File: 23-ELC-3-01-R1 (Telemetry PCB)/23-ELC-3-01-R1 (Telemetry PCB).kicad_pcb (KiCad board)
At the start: 2 copper layers, 56.5 x 65 mm, 117 parts, among them J1 Conn_01x01, J11 LHRE_Component_Library_Raspbe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, J2 Conn_01x02, J3 Conn_01x08, J4 Conn_01x02, J5 Conn_01x02, J6 Conn_01x08, J7 Conn_01x02, J8 Conn_02x11_Top_Bottom, J9 Conn_01x06, SW1 SW_DPDT_x2, U1 LHRE_Component_Library_Adafru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, U10 MCP2515-xSO, U11 SN65HVD230, U2 DS3231M, U3 LMR51420, U4 MCP2515-xSO, U5 SN65HVD230, U6 MCP2515-xSO, U7 SN65HVD230, U8 MCP2515-xSO, U9 SN65HVD230, Y1 16 MHz, Y2 16 MHz, Y3 16 MHz, Y4 16 MHz

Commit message: First draft of layout
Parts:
- removed J2, J4, J5, J7: Conn_01x02, Connector_PinHeader_2.54mm:PinHeader_1x02_P2.54mm_Vertical
- added C29: 1uF, Capacitor_SMD:C_0805_2012Metric_Pad1.18x1.45mm_HandSolder, B.Cu at (131.2, 82.2)
- added C30: 1uF, Capacitor_SMD:C_0805_2012Metric_Pad1.18x1.45mm_HandSolder, B.Cu at (116.7, 82.8)
- C3, C4, C5, C6, C7, C8, F1, L1, R4, R5, R7, R8, R9, U2, U3: moved to B.Cu
- moved C21 253.0 mm to (116.0, 127.4), turned to -90 degrees
- moved TP22 248.7 mm to (133.7, 128.4)
- moved C23 244.4 mm to (146.0, 125.0)
- moved R20 244.2 mm to (116.0, 122.3), turned to -90 degrees
- moved Y3 242.3 mm to (135.1, 120.8), turned to -135 degrees
- moved C5 240.6 mm to (144.4, 81.2)
- moved C8 238.9 mm to (138.8, 77.4)
- moved C19 237.8 mm to (132.1, 122.9), turned to -45 degrees
- moved JP11 237.1 mm to (142.7, 122.3), turned to 90 degrees
- moved JP9 235.3 mm to (130.7, 125.5)
- moved C3 234.7 mm to (144.4, 79.7)
- moved JP10 232.9 mm to (130.7, 128.0), turned to 180 degrees
- moved R7 232.2 mm to (144.4, 88.2)
- moved C22 231.9 mm to (135.6, 126.8), turned to -90 degrees
- moved C4 229.0 mm to (144.4, 78.2)
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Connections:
- J9 pad 4: /TSAL_G -> GND
- J9 pad 5: /TSAL_R -> /TSAL_G
- J9 pad 6: unconnected-(J9-Pad6) -> /TSAL_R
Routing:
- net +3V3: track 0.00 -> 230.6 mm, vias 0 -> 10
- net +5V: track 0.00 -> 162.3 mm, vias 0 -> 4
- net GND: track 0.00 -> 145.8 mm, vias 0 -> 39
- net /GPS_RX: track 0.00 -> 79.6 mm
- net +BATT: track 0.00 -> 70.4 mm
- net /GPS_TX: track 0.00 -> 69.9 mm
- net /CAN_CS_2: track 0.00 -> 66.7 mm, vias 0 -> 3
- net /CAN_MISO_01: track 0.00 -> 56.7 mm, vias 0 -> 4
- net /CAN_CS_3: track 0.00 -> 48.9 mm
- net /TSAL_R: track 0.00 -> 48.4 mm, vias 0 -> 1
- net /CAN_L_1_A: track 0.00 -> 46.5 mm, vias 0 -> 2
- net /CAN_SCK_01: track 0.00 -> 45.8 mm, vias 0 -> 3
- net /CAN_CS_0: track 0.00 -> 44.1 mm, vias 0 -> 3
- net /CAN_MISO_23: track 0.00 -> 43.3 mm, vias 0 -> 3
- net /CAN_H_1: track 0.00 -> 41.6 mm, vias 0 -> 2
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- added copper zone on B.Cu, net GND

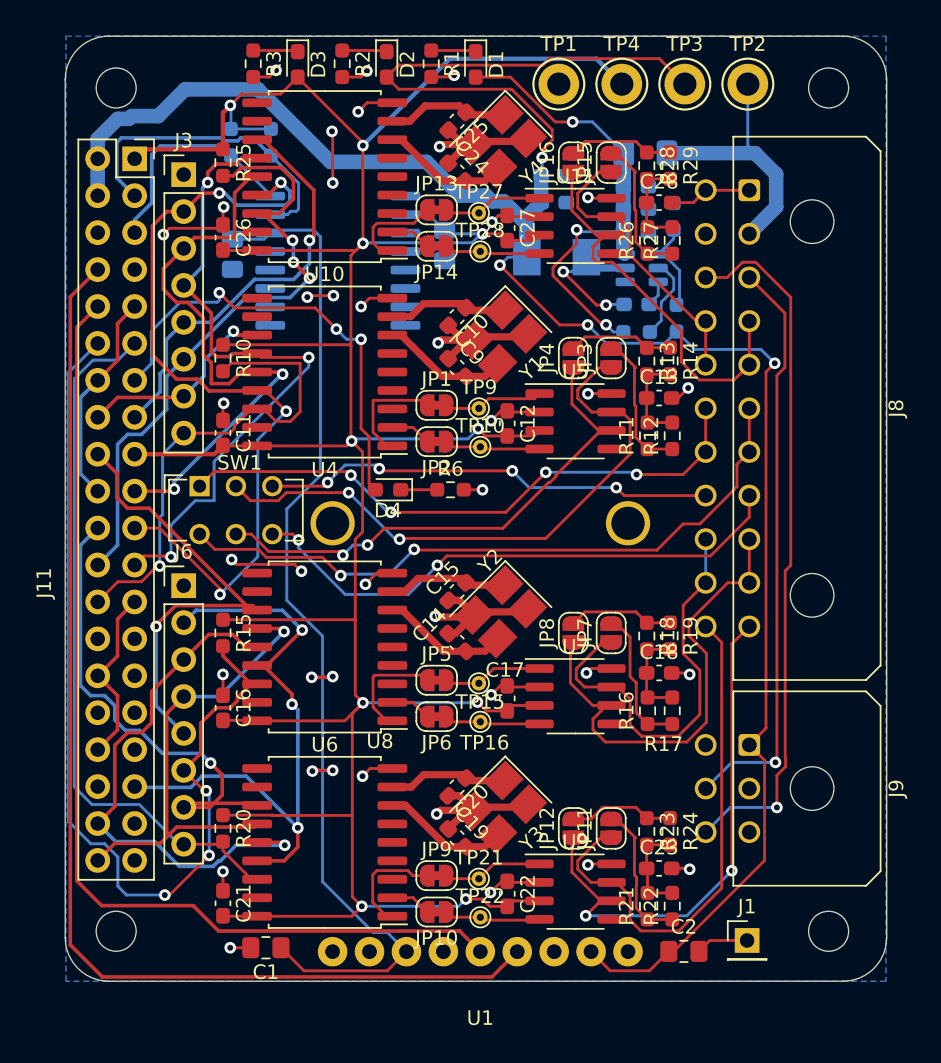
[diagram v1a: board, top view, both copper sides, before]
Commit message: Fixed review notes and made 4 layer
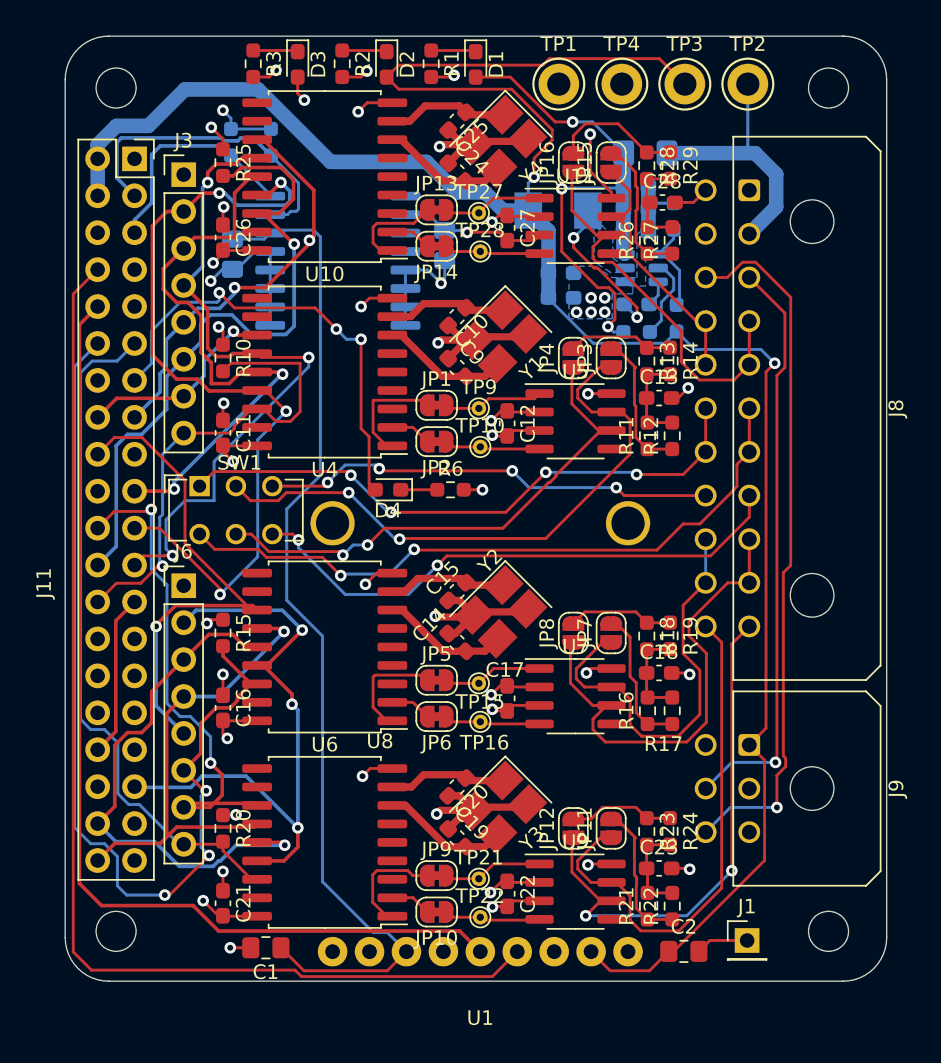
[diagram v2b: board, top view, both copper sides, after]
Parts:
- moved C8 6.72 mm to (139.2, 84.1)
- moved C7 6.57 mm to (139.2, 85.8)
- moved L1 3.20 mm to (139.1, 79.8)
- moved C28 0.23 mm to (146.2, 79.2)
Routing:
- net +3V3: track 230.6 -> 47.0 mm, vias 10 -> 14
- net GND: track 145.8 -> 135.6 mm, vias 39 -> 35
- net +5V: track 162.3 -> 154.7 mm, vias 4 -> 2
- net /Buck 24 to 5/V_in: track 32.9 -> 36.5 mm
- net /CAN_INT_2: track 32.3 -> 34.8 mm
- net /Buck 24 to 5/SW: track 10.1 -> 12.6 mm
- net /CAN_CS_0: track 44.1 -> 46.3 mm, vias 3 -> 1
- net /CAN_H_0: track 19.9 -> 18.0 mm
- net Net-(JP16-Pad2): track 7.30 -> 9.01 mm
- net /CAN_CS_3: track 48.9 -> 47.7 mm
- net /CAN_SCK_01: track 45.8 -> 46.6 mm
- net /CAN_INT_3: track 33.8 -> 34.5 mm, vias 1 -> 2
- net /CAN_INT_0: track 28.8 -> 28.2 mm, vias 1 -> 2
- added copper zone on In2.Cu, net +3V3
- added copper zone on B.Cu, net /Buck 24 to 5/SW
- added copper zone on In1.Cu, net GND
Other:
- copper layers 2 -> 4

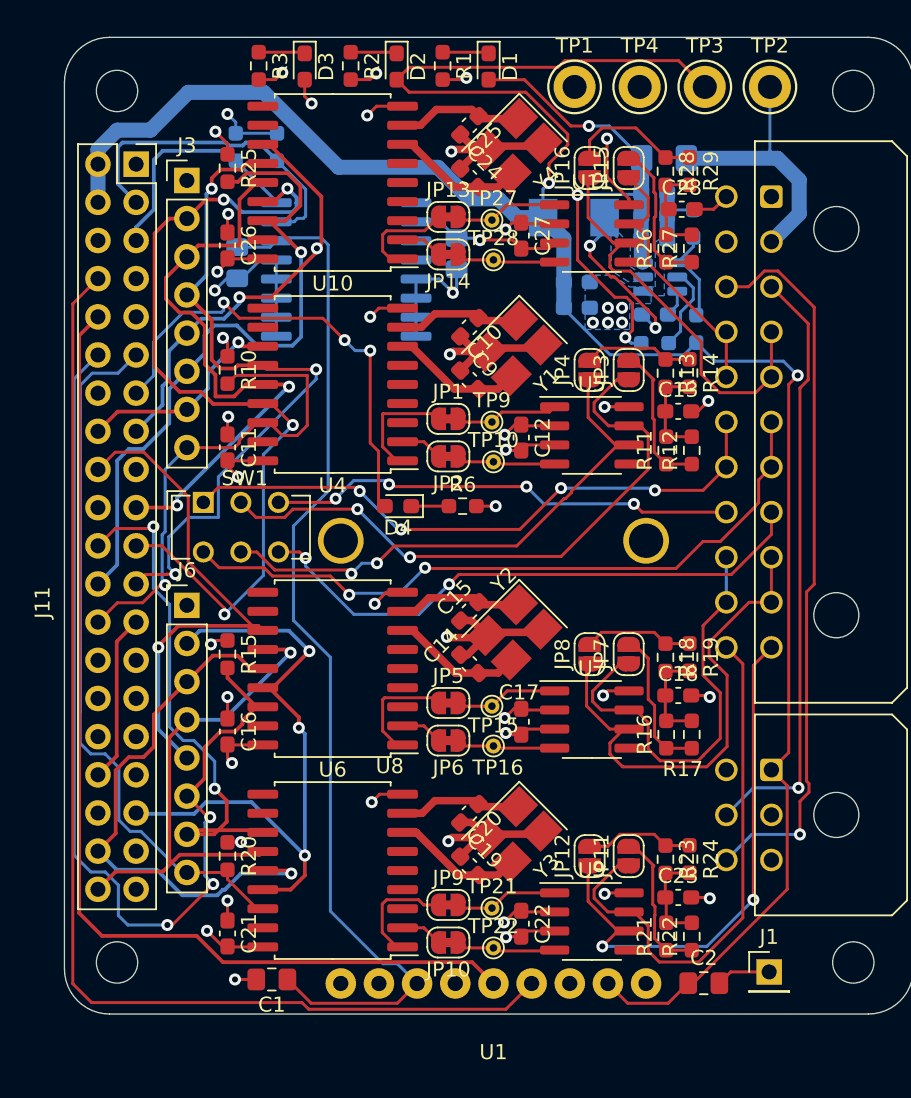
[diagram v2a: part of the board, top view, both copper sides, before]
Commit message: Changes for reference legibility, trace clearance, and through hole solder mask
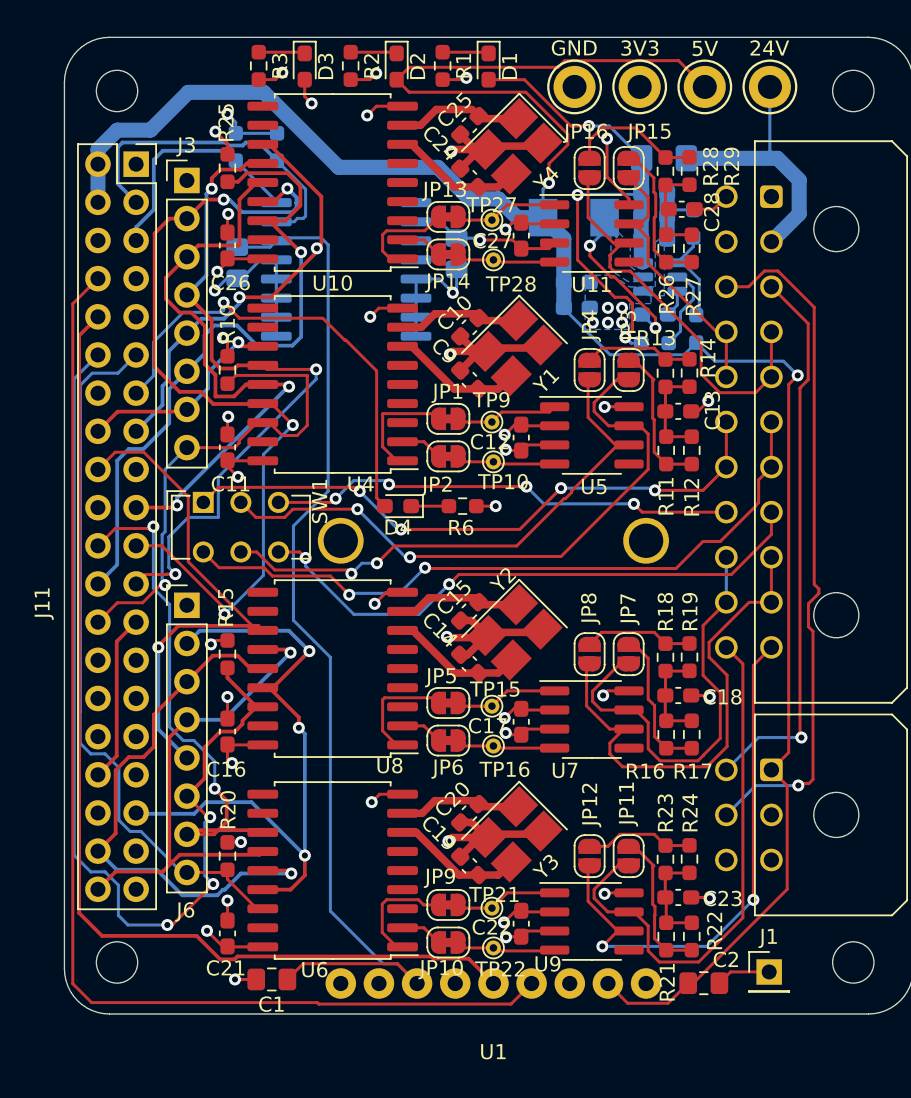
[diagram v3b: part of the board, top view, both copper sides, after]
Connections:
- J9 pad 4: GND -> /TSAL_G
- J9 pad 5: /TSAL_G -> /TSAL_R
- J9 pad 6: /TSAL_R -> unconnected-(J9-Pad6)
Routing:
- net /TSAL_G: track 40.2 -> 37.2 mm
- net /TSAL_R: track 48.5 -> 46.0 mm
- net Net-(D4-Pad2): track 31.8 -> 31.2 mm, vias 3 -> 1
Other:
- board text added: "24V"
- board text added: "3V3"
- board text added: "5V"
- board text added: "GND"
